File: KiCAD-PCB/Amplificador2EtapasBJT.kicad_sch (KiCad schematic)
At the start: 38 parts, among them J1 Vin, J2 CC, J3 Vout, Q1 NPN, Q2 NPN, Q3 NPN, Q4 NPN, Q5 PNP

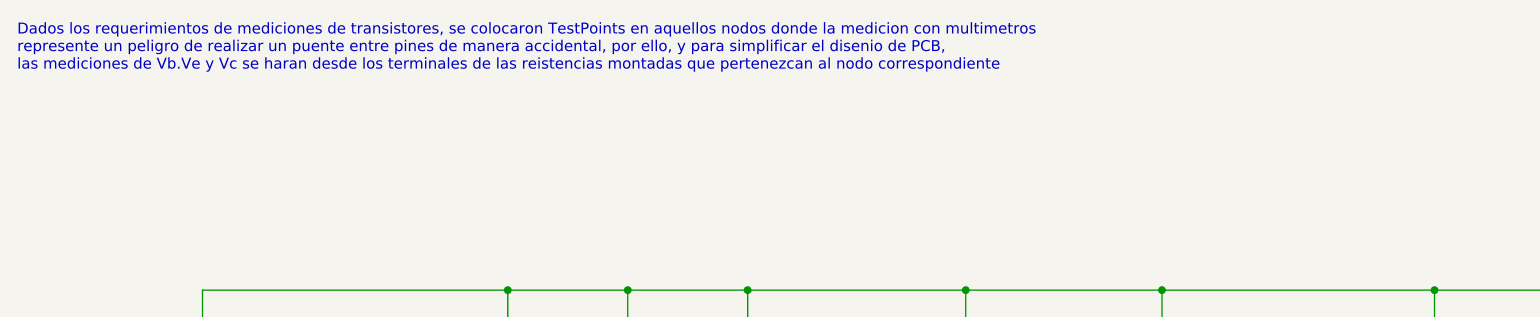
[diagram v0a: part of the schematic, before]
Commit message: Correccion de Esquematico y PCB
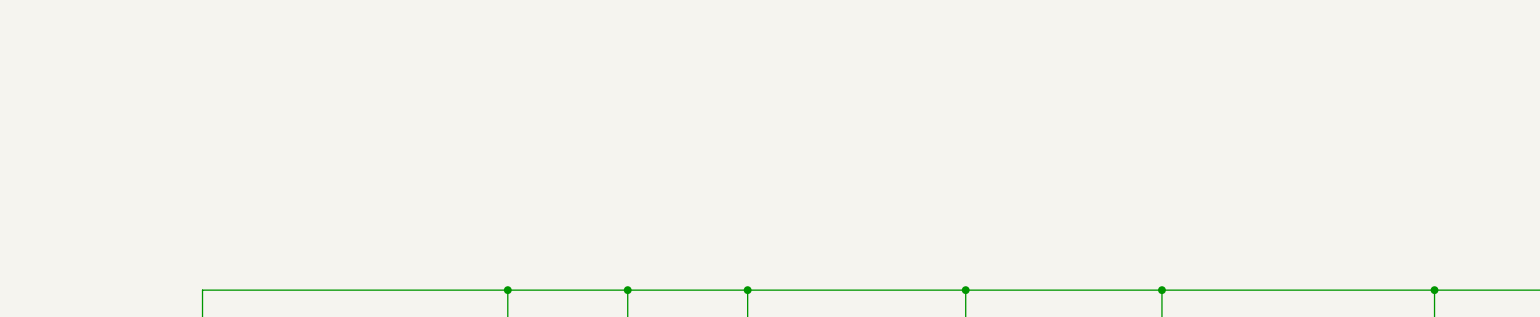
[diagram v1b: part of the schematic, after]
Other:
- note removed: "Dados los requerimientos de mediciones de transistores, se colocaron TestPoints en aquellos nodos donde la medicion con multimetros represente un peligro de realizar un puente entre pines de manera accidental, por ello, y para simplificar el disenio de PCB, las mediciones de Vb.Ve y Vc se haran desde los terminales de las reistencias montadas que pertenezcan al nodo correspondiente"
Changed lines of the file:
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@@
     (stroke (width 0) (type default))
-  )
-  (text "Dados los requerimientos de mediciones de transistores, se colocaron TestPoints en aquellos nodos donde la medicion con multimetros \nrepresente un peligro de realizar un puente entre pines de manera accidental, por ello, y para simplificar el disenio de PCB, \nlas mediciones de Vb.Ve y Vc se haran desde los terminales de las reistencias montadas que pertenezcan al nodo correspondiente"
-    (at 15.24 21.59 0)
-    (effects (font (size 1.27 1.27)) (justify left bottom))
   )
   (symbol (lib_id "Connector:Screw_Terminal_01x02") (at 248.92 93.98 0) (unit 1)

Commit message: Actualizacion del Sch y PCB a corregir
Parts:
- removed Ce1: 33uF, Capacitor_THT:CP_Radial_D6.3mm_P2.50mm, symbol Device:C
- removed Co1, Co2: 10uF, Capacitor_THT:CP_Radial_D6.3mm_P2.50mm, symbol Device:C
- removed TP3: TPBQ5, Connector_PinHeader_2.54mm:PinHeader_1x01_P2.54mm_Vertical, symbol Connector:TestPoint
- removed TP6: TPB2E1, Connector_PinSocket_2.54mm:PinSocket_1x02_P2.54mm_Vertical, symbol Connector:TestPoint_2Pole
- added C1: 100nF, symbol Device:C
- added Ce1: 33uF, Capacitor_THT:CP_Radial_D6.3mm_P2.50mm, symbol Device:C_Polarized
- added Ci2: 1000uF, Capacitor_THT:CP_Radial_D10.0mm_P5.00mm, symbol Device:C
- added Co2: 10uF, Capacitor_THT:CP_Radial_Tantal_D6.0mm_P5.00mm, symbol Device:C_Polarized
- added Co3: 1000uF, Capacitor_THT:CP_Radial_D6.3mm_P2.50mm, symbol Device:C_Polarized
- added RBQ4: 100, Resistor_THT:R_Axial_DIN0207_L6.3mm_D2.5mm_P10.16mm_Horizontal, symbol Device:R
- added Rout2: 15, Resistor_THT:R_Axial_DIN0207_L6.3mm_D2.5mm_P10.16mm_Horizontal, symbol Device:R
- added Rout3: 10, Resistor_THT:R_Axial_DIN0207_L6.3mm_D2.5mm_P10.16mm_Horizontal, symbol Device:R
- added TP4: TPB-Q2, Connector_PinHeader_2.54mm:PinHeader_1x01_P2.54mm_Vertical, symbol Connector:TestPoint
- Q1: value NPN -> BC546 B NPN; footprint Package_TO_SOT_THT:TO-92L_Inline_Wide -> Package_TO_SOT_THT:TO-92_Inline_Wide
- Q2: value NPN -> BD 139NPN; footprint Package_TO_SOT_THT:TO-92L_Inline_Wide -> Package_TO_SOT_THT:TO-126-3_Vertical
- Q3: footprint Package_TO_SOT_THT:TO-92L_Inline_Wide -> Package_TO_SOT_THT:TO-92_Inline_Wide
- Q4: footprint Package_TO_SOT_THT:TO-92L_Inline_Wide -> Package_TO_SOT_THT:TO-220-3_Vertical
- Q5: footprint Package_TO_SOT_THT:TO-126-3_Vertical -> Package_TO_SOT_THT:TO-220-3_Vertical
- REQ2: value 470 -> 47
- Rout1: value 7.5 -> 15; footprint Resistor_THT:R_Axial_DIN0414_L11.9mm_D4.5mm_P15.24mm_Horizontal -> Resistor_THT:R_Axial_DIN0207_L6.3mm_D2.5mm_P10.16mm_Horizontal
- renumbered Cc1 to Co1
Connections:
- net Earth: now also J3.1 (Pin_1), C1.2, Ce1.2, Ci2.1; no longer J3.2 (Pin_2)
- net at JP9.2 (B), RL1.1: now also J3.2 (Pin_2); no longer J3.1 (Pin_1)
- net at J2.2 (Pin_2), JP1.1 (A), JP10.1 (A)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: now also Ci2.2
- net at Q3.3 (E), RE1Q3.1: now also Ce1.1
- net at Q4.3 (E), Q5.1 (C), REQ4.1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: now also Rout2.1
- net at Q4.1 (C): now also RBQ4.2; no longer Q5.2 (B)
- net at JP8.2 (B): now also Co2.2
- net at Q4.2 (B), R1Q4.1, R2Q4.2: now also Co2.1
- net at Q1.3 (E), Q2.2 (B): now also TP4.1
- net at Rout1.2: now also Co3.1, Rout2.2, Rout3.2
- net at JP9.1 (A): now also Co3.2
- new net: C1.1, Rout3.1
- new net: Q5.2 (B), RBQ4.1
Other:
- moved on the sheet: J3, JP10, JP7, R1Q4, R2Q4, Rout1

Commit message: Imagenes del Setup de Proteus
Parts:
- removed C1: 100nF, symbol Device:C
- removed Rout3: 10, Resistor_THT:R_Axial_DIN0207_L6.3mm_D2.5mm_P10.16mm_Horizontal, symbol Device:R
- added Ci3: 100pF, Capacitor_THT:CP_Radial_D6.3mm_P2.50mm, symbol Device:C
- Ci2: value 1000uF -> 10uF
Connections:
- net at Co2.1, Q4.2 (B), R1Q4.1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: now also Ci3.1
- net at Q4.1 (C), RBQ4.2: now also Ci3.2
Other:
- moved on the sheet: Co3
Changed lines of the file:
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@@
   (junction (at 125.73 78.74) (diameter 0) (color 0 0 0 0)
   )
+  (junction (at 191.77 67.31) (diameter 0) (color 0 0 0 0)
+  )
   (junction (at 148.59 95.25) (diameter 0) (color 0 0 0 0)
   )
@@
   (junction (at 36.83 67.31) (diameter 0) (color 0 0 0 0)
   )
-  (junction (at 222.25 80.01) (diameter 0) (color 0 0 0 0)
-  )
   (junction (at 191.77 80.01) (diameter 0) (color 0 0 0 0)
   )
   (junction (at 210.82 80.01) (diameter 0) (color 0 0 0 0)
   )
+  (junction (at 177.8 67.31) (diameter 0) (color 0 0 0 0)
+  )
   (junction (at 125.73 107.95) (diameter 0) (color 0 0 0 0)
   )
@@
   (junction (at 177.8 46.99) (diameter 0) (color 0 0 0 0)
   )
-  (junction (at 222.25 107.95) (diameter 0) (color 0 0 0 0)
-  )
   (junction (at 100.33 46.99) (diameter 0) (color 0 0 0 0)
   )
@@
     (stroke (width 0) (type default))
   )
-  (wire (pts (xy 229.87 78.74) (xy 229.87 83.82))
+  (wire (pts (xy 229.87 80.01) (xy 229.87 83.82))
     (stroke (width 0) (type default))
   )
@@
     (stroke (width 0) (type default))
   )
-  (wire (pts (xy 222.25 80.01) (xy 222.25 78.74))
-    (stroke (width 0) (type default))
-  )
   (wire (pts (xy 100.33 46.99) (xy 125.73 46.99))
     (stroke (width 0) (type default))
@@
     (stroke (width 0) (type default))
   )
-  (wire (pts (xy 222.25 104.14) (xy 222.25 107.95))
-    (stroke (width 0) (type default))
-  )
   (wire (pts (xy 58.42 100.33) (xy 58.42 107.95))
     (stroke (width 0) (type default))
@@
     (stroke (width 0) (type default))
   )
+  (wire (pts (xy 187.96 67.31) (xy 191.77 67.31))
+    (stroke (width 0) (type default))
+  )
   (wire (pts (xy 125.73 107.95) (xy 148.59 107.95))
     (stroke (width 0) (type default))
@@
     (stroke (width 0) (type default))
   )
-  (wire (pts (xy 191.77 107.95) (xy 222.25 107.95))
-    (stroke (width 0) (type default))
-  )
   (wire (pts (xy 229.87 107.95) (xy 250.19 107.95))
     (stroke (width 0) (type default))
@@
     (stroke (width 0) (type default))
   )
-  (wire (pts (xy 177.8 59.69) (xy 177.8 73.66))
+  (wire (pts (xy 177.8 67.31) (xy 180.34 67.31))
+    (stroke (width 0) (type default))
+  )
+  (wire (pts (xy 177.8 59.69) (xy 177.8 67.31))
     (stroke (width 0) (type default))
   )
@@
     (stroke (width 0) (type default))
   )
-  (wire (pts (xy 222.25 80.01) (xy 222.25 83.82))
-    (stroke (width 0) (type default))
-  )
   (wire (pts (xy 250.19 99.06) (xy 250.19 107.95))
     (stroke (width 0) (type default))
@@
     (stroke (width 0) (type default))
   )
-  (wire (pts (xy 222.25 91.44) (xy 222.25 96.52))
-    (stroke (width 0) (type default))
-  )
   (wire (pts (xy 86.36 91.44) (xy 86.36 95.25))
     (stroke (width 0) (type default))
@@
     (stroke (width 0) (type default))
   )
+  (wire (pts (xy 177.8 67.31) (xy 177.8 73.66))
+    (stroke (width 0) (type default))
+  )
   (wire (pts (xy 158.75 107.95) (xy 148.59 107.95))
     (stroke (width 0) (type default))
@@
     (stroke (width 0) (type default))
   )
-  (wire (pts (xy 222.25 107.95) (xy 229.87 107.95))
+  (wire (pts (xy 191.77 107.95) (xy 229.87 107.95))
     (stroke (width 0) (type default))
   )
@@
     )
   )
-  (symbol (lib_id "Device:C") (at 222.25 100.33 0) (unit 1)
-    (in_bom yes) (on_board yes) (dnp no)
-    (property "Reference" "C1" (at 226.06 99.06 0)
-      (effects (font (size 1.27 1.27)) (justify left))
-    )
-    (property "Value" "100nF" (at 215.9 102.87 0)
-      (effects (font (size 1.27 1.27)) (justify left))
-    )
-    (property "Footprint" "" (at 223.2152 104.14 0)
-      (effects (font (size 1.27 1.27)) hide)
-    )
-    (property "Datasheet" "~" (at 222.25 100.33 0)
-      (effects (font (size 1.27 1.27)) hide)
-    )
-    (pin "1")
-    (pin "2")
-    (instances
-      (project "Amplificador2EtapasBJT"
-        (path "/6c0ee505-22c4-4584-aa99-ccf325259f94"
-          (reference "C1") (unit 1)
-        )
-      )
-    )
-  )
   (symbol (lib_id "Jumper:Jumper_2_Bridged") (at 133.35 78.74 0) (unit 1)
     (in_bom yes) (on_board yes) (dnp no)
@@
   )
   (symbol (lib_id "Device:C_Polarized") (at 172.72 73.66 270) (unit 1)
-    (in_bom yes) (on_board yes) (dnp no) (fields_autoplaced)
-    (property "Reference" "Co2" (at 173.609 66.04 90)
+    (in_bom yes) (on_board yes) (dnp no)
+    (property "Reference" "Co2" (at 171.45 66.04 90)
       (effects (font (size 1.27 1.27)))
     )
@@
       (effects (font (size 1.27 1.27)) (justify right))
     )
-    (property "Value" "1000uF" (at 46.99 72.39 0)
+    (property "Value" "10uF" (at 46.99 72.39 0)
       (effects (font (size 1.27 1.27)) (justify right))
     )
@@
     )
   )
-  (symbol (lib_id "Device:R") (at 222.25 87.63 180) (unit 1)
-    (in_bom yes) (on_board yes) (dnp no)
-    (property "Reference" "Rout3" (at 224.79 87.63 90)
-      (effects (font (size 1.27 1.27)))
-    )
-    (property "Value" "10" (at 222.25 88.9 90)
-      (effects (font (size 1.27 1.27)))
-    )
-    (property "Footprint" "Resistor_THT:R_Axial_DIN0207_L6.3mm_D2.5mm_P10.16mm_Horizontal" (at 224.028 87.63 90)
-      (effects (font (size 1.27 1.27)) hide)
-    )
-    (property "Datasheet" "~" (at 222.25 87.63 0)
-      (effects (font (size 1.27 1.27)) hide)
-    )
-    (pin "1")
-    (pin "2")
-    (instances
-      (project "Amplificador2EtapasBJT"
-        (path "/6c0ee505-22c4-4584-aa99-ccf325259f94"
-          (reference "Rout3") (unit 1)
+  (symbol (lib_id "Device:C") (at 184.15 67.31 90) (unit 1)
+    (in_bom yes) (on_board yes) (dnp no)
+    (property "Reference" "Ci3" (at 180.34 66.04 90)
+      (effects (font (size 1.27 1.27)))
+    )
+    (property "Value" "100pF" (at 184.15 63.5 90)
+      (effects (font (size 1.27 1.27)))
+    )
+    (property "Footprint" "Capacitor_THT:CP_Radial_D6.3mm_P2.50mm" (at 187.96 66.3448 0)
+      (effects (font (size 1.27 1.27)) hide)
+    )
+    (property "Datasheet" "~" (at 184.15 67.31 0)
+      (effects (font (size 1.27 1.27)) hide)
+    )
+    (pin "2")
+    (pin "1")
+    (instances
+      (project "Amplificador2EtapasBJT"
+        (path "/6c0ee505-22c4-4584-aa99-ccf325259f94"
+          (reference "Ci3") (unit 1)
         )
       )
@@
     )
   )
-  (symbol (lib_id "Device:C_Polarized") (at 226.06 78.74 90) (unit 1)
-    (in_bom yes) (on_board yes) (dnp no) (fields_autoplaced)
-    (property "Reference" "Co3" (at 225.171 71.12 90)
-      (effects (font (size 1.27 1.27)))
-    )
-    (property "Value" "1000uF" (at 225.171 73.66 90)
-      (effects (font (size 1.27 1.27)))
-    )
-    (property "Footprint" "Capacitor_THT:CP_Radial_D6.3mm_P2.50mm" (at 229.87 77.7748 0)
-      (effects (font (size 1.27 1.27)) hide)
-    )
-    (property "Datasheet" "~" (at 226.06 78.74 0)
-      (effects (font (size 1.27 1.27)) hide)
-    )
+  (symbol (lib_id "Device:C_Polarized") (at 226.06 80.01 90) (unit 1)
+    (in_bom yes) (on_board yes) (dnp no) (fields_autoplaced)
+    (property "Reference" "Co3" (at 225.171 72.39 90)
+      (effects (font (size 1.27 1.27)))
+    )
+    (property "Value" "1000uF" (at 225.171 74.93 90)
+      (effects (font (size 1.27 1.27)))
+    )
+    (property "Footprint" "Capacitor_THT:CP_Radial_D6.3mm_P2.50mm" (at 229.87 79.0448 0)
+      (effects (font (size 1.27 1.27)) hide)
+    )
+    (property "Datasheet" "~" (at 226.06 80.01 0)
+      (effects (font (size 1.27 1.27)) hide)
+    )

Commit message: pusheo un monotn de cosas
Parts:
- removed Rout2: 15, Resistor_THT:R_Axial_DIN0207_L6.3mm_D2.5mm_P10.16mm_Horizontal, symbol Device:R
- Rout1: value 15 -> 10
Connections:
- net at Ci3.1, Q4.2 (B), R1Q4.1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: now also JP8.2 (B); no longer Co2.1
- net at Co2.2: now also Q3.1 (C), RC1.2; no longer JP8.2 (B)
- new net: Co2.1, JP8.1 (A)
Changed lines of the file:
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@@
   (junction (at 191.77 80.01) (diameter 0) (color 0 0 0 0)
   )
-  (junction (at 210.82 80.01) (diameter 0) (color 0 0 0 0)
-  )
   (junction (at 177.8 67.31) (diameter 0) (color 0 0 0 0)
   )
@@
   (junction (at 72.39 46.99) (diameter 0) (color 0 0 0 0)
   )
-  (junction (at 218.44 80.01) (diameter 0) (color 0 0 0 0)
-  )
   (junction (at 177.8 46.99) (diameter 0) (color 0 0 0 0)
   )
@@
     (stroke (width 0) (type default))
   )
+  (wire (pts (xy 162.56 73.66) (xy 166.37 73.66))
+    (stroke (width 0) (type default))
+  )
   (wire (pts (xy 209.55 80.01) (xy 210.82 80.01))
     (stroke (width 0) (type default))
@@
     (stroke (width 0) (type default))
   )
-  (wire (pts (xy 218.44 80.01) (xy 218.44 87.63))
-    (stroke (width 0) (type default))
-  )
   (wire (pts (xy 86.36 86.36) (xy 86.36 91.44))
     (stroke (width 0) (type default))
@@
     (stroke (width 0) (type default))
   )
-  (wire (pts (xy 210.82 80.01) (xy 210.82 87.63))
-    (stroke (width 0) (type default))
-  )
   (wire (pts (xy 72.39 81.28) (xy 78.74 81.28))
     (stroke (width 0) (type default))
@@
     (stroke (width 0) (type default))
   )
-  (wire (pts (xy 165.1 73.66) (xy 168.91 73.66))
-    (stroke (width 0) (type default))
-  )
   (wire (pts (xy 148.59 46.99) (xy 125.73 46.99))
     (stroke (width 0) (type default))
@@
     )
   )
-  (symbol (lib_id "Device:C_Polarized") (at 172.72 73.66 270) (unit 1)
-    (in_bom yes) (on_board yes) (dnp no)
-    (property "Reference" "Co2" (at 171.45 66.04 90)
-      (effects (font (size 1.27 1.27)))
-    )
-    (property "Value" "10uF" (at 173.609 68.58 90)
-      (effects (font (size 1.27 1.27)))
-    )
-    (property "Footprint" "Capacitor_THT:CP_Radial_Tantal_D6.0mm_P5.00mm" (at 168.91 74.6252 0)
-      (effects (font (size 1.27 1.27)) hide)
-    )
-    (property "Datasheet" "~" (at 172.72 73.66 0)
+  (symbol (lib_id "Jumper:Jumper_2_Bridged") (at 100.33 59.69 270) (unit 1)
+    (in_bom yes) (on_board yes) (dnp no)
+    (property "Reference" "JP3" (at 102.87 58.42 90)
+      (effects (font (size 1.27 1.27)) (justify left))
+    )
+    (property "Value" "C-Q2" (at 102.87 60.96 90)
+      (effects (font (size 1.27 1.27)) (justify left))
+    )
+    (property "Footprint" "Connector_PinHeader_2.54mm:PinHeader_1x02_P2.54mm_Vertical" (at 100.33 59.69 0)
+      (effects (font (size 1.27 1.27)) hide)
+    )
+    (property "Datasheet" "~" (at 100.33 59.69 0)
+      (effects (font (size 1.27 1.27)) hide)
+    )
+    (pin "2")
+    (pin "1")
+    (instances
+      (project "Amplificador2EtapasBJT"
+        (path "/6c0ee505-22c4-4584-aa99-ccf325259f94"
+          (reference "JP3") (unit 1)
+        )
+      )
+    )
+  )
+  (symbol (lib_id "Device:C_Polarized") (at 158.75 73.66 270) (unit 1)
+    (in_bom yes) (on_board yes) (dnp no)
+    (property "Reference" "Co2" (at 157.48 66.04 90)
+      (effects (font (size 1.27 1.27)))
+    )
+    (property "Value" "10uF" (at 159.639 68.58 90)
+      (effects (font (size 1.27 1.27)))
+    )
+    (property "Footprint" "Capacitor_THT:CP_Radial_Tantal_D6.0mm_P5.00mm" (at 154.94 74.6252 0)
+      (effects (font (size 1.27 1.27)) hide)
+    )
+    (property "Datasheet" "~" (at 158.75 73.66 0)
       (effects (font (size 1.27 1.27)) hide)
     )
@@
         (path "/6c0ee505-22c4-4584-aa99-ccf325259f94"
           (reference "Co2") (unit 1)
-        )
-      )
-    )
-  )
-  (symbol (lib_id "Jumper:Jumper_2_Bridged") (at 100.33 59.69 270) (unit 1)
-    (in_bom yes) (on_board yes) (dnp no)
-    (property "Reference" "JP3" (at 102.87 58.42 90)
-      (effects (font (size 1.27 1.27)) (justify left))
-    )
-    (property "Value" "C-Q2" (at 102.87 60.96 90)
-      (effects (font (size 1.27 1.27)) (justify left))
-    )
-    (property "Footprint" "Connector_PinHeader_2.54mm:PinHeader_1x02_P2.54mm_Vertical" (at 100.33 59.69 0)
-      (effects (font (size 1.27 1.27)) hide)
-    )
-    (property "Datasheet" "~" (at 100.33 59.69 0)
-      (effects (font (size 1.27 1.27)) hide)
-    )
-    (pin "2")
-    (pin "1")
-    (instances
-      (project "Amplificador2EtapasBJT"
-        (path "/6c0ee505-22c4-4584-aa99-ccf325259f94"
-          (reference "JP3") (unit 1)
         )
       )
@@
     )
   )
+  (symbol (lib_id "Jumper:Jumper_2_Bridged") (at 171.45 73.66 0) (unit 1)
+    (in_bom yes) (on_board yes) (dnp no)
+    (property "Reference" "JP8" (at 168.91 76.2 0)
+      (effects (font (size 1.27 1.27)) (justify left))
+    )
+    (property "Value" "FinEtapa2" (at 167.64 71.12 0)
+      (effects (font (size 1.27 1.27)) (justify left))
+    )
+    (property "Footprint" "Connector_PinHeader_2.54mm:PinHeader_1x02_P2.54mm_Vertical" (at 171.45 73.66 0)
+      (effects (font (size 1.27 1.27)) hide)
+    )
+    (property "Datasheet" "~" (at 171.45 73.66 0)
+      (effects (font (size 1.27 1.27)) hide)
+    )
+    (pin "2")
+    (pin "1")
+    (instances
+      (project "Amplificador2EtapasBJT"
+        (path "/6c0ee505-22c4-4584-aa99-ccf325259f94"
+          (reference "JP8") (unit 1)
+        )
+      )
+    )
+  )
   (symbol (lib_id "Simulation_SPICE:NPN") (at 189.23 73.66 0) (unit 1)
     (in_bom yes) (on_board yes) (dnp no) (fields_autoplaced)
@@
       (effects (font (size 1.27 1.27)))
     )
-    (property "Value" "15" (at 214.63 77.47 90)
+    (property "Value" "10" (at 214.63 77.47 90)
       (effects (font (size 1.27 1.27)))
     )
@@
         )
       )
-    )
-  )
-  (symbol (lib_id "Device:R") (at 214.63 87.63 90) (unit 1)
-    (in_bom yes) (on_board yes) (dnp no)
-    (property "Reference" "Rout2" (at 214.63 90.17 90)
-      (effects (font (size 1.27 1.27)))
-    )
-    (property "Value" "15" (at 214.63 85.09 90)
-      (effects (font (size 1.27 1.27)))
-    )
-    (property "Footprint" "Resistor_THT:R_Axial_DIN0207_L6.3mm_D2.5mm_P10.16mm_Horizontal" (at 214.63 89.408 90)
-      (effects (font (size 1.27 1.27)) hide)
-    )
-    (property "Datasheet" "~" (at 214.63 87.63 0)
-      (effects (font (size 1.27 1.27)) hide)
-    )
-    (pin "1")
-    (pin "2")
-    (instances
-      (project "Amplificador2EtapasBJT"
-        (path "/6c0ee505-22c4-4584-aa99-ccf325259f94"
-          (reference "Rout2") (unit 1)
-        )
-      )
-    )
-  )
-  (symbol (lib_id "Jumper:Jumper_2_Bridged") (at 160.02 73.66 0) (unit 1)
-    (in_bom yes) (on_board yes) (dnp no)
-    (property "Reference" "JP8" (at 157.48 76.2 0)
-      (effects (font (size 1.27 1.27)) (justify left))
-    )
-    (property "Value" "FinEtapa2" (at 156.21 71.12 0)
-      (effects (font (size 1.27 1.27)) (justify left))
-    )
-    (property "Footprint" "Connector_PinHeader_2.54mm:PinHeader_1x02_P2.54mm_Vertical" (at 160.02 73.66 0)
-      (effects (font (size 1.27 1.27)) hide)
-    )
-    (property "Datasheet" "~" (at 160.02 73.66 0)
-      (effects (font (size 1.27 1.27)) hide)
-    )
-    (pin "2")
-    (pin "1")
-    (instances
-      (project "Amplificador2EtapasBJT"
-        (path "/6c0ee505-22c4-4584-aa99-ccf325259f94"
-          (reference "JP8") (unit 1)
-        )
-      )
